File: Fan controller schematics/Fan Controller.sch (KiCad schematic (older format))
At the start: 9 parts, among them IC1 ATMEGA328-P, SW1 ROTARY_ENCODER, Y1 16MHz

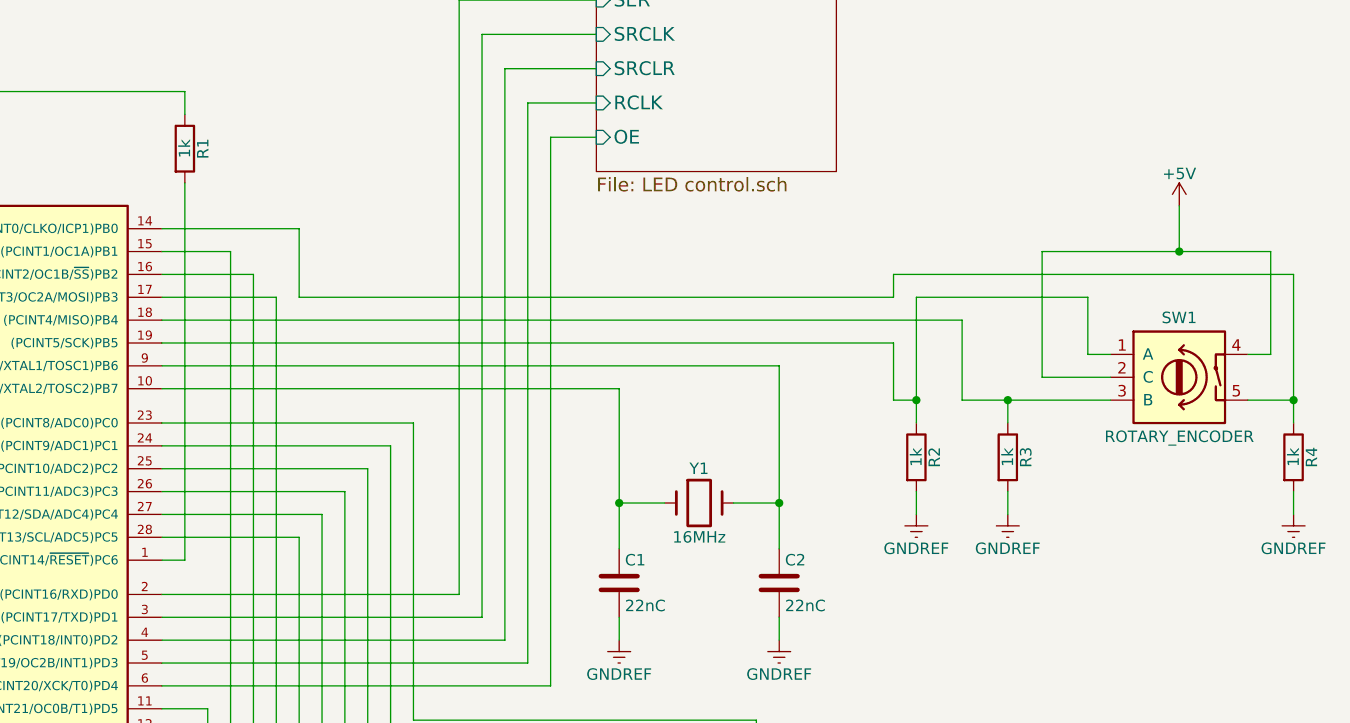
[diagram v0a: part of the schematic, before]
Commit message: Change rotary encoder to GND ref
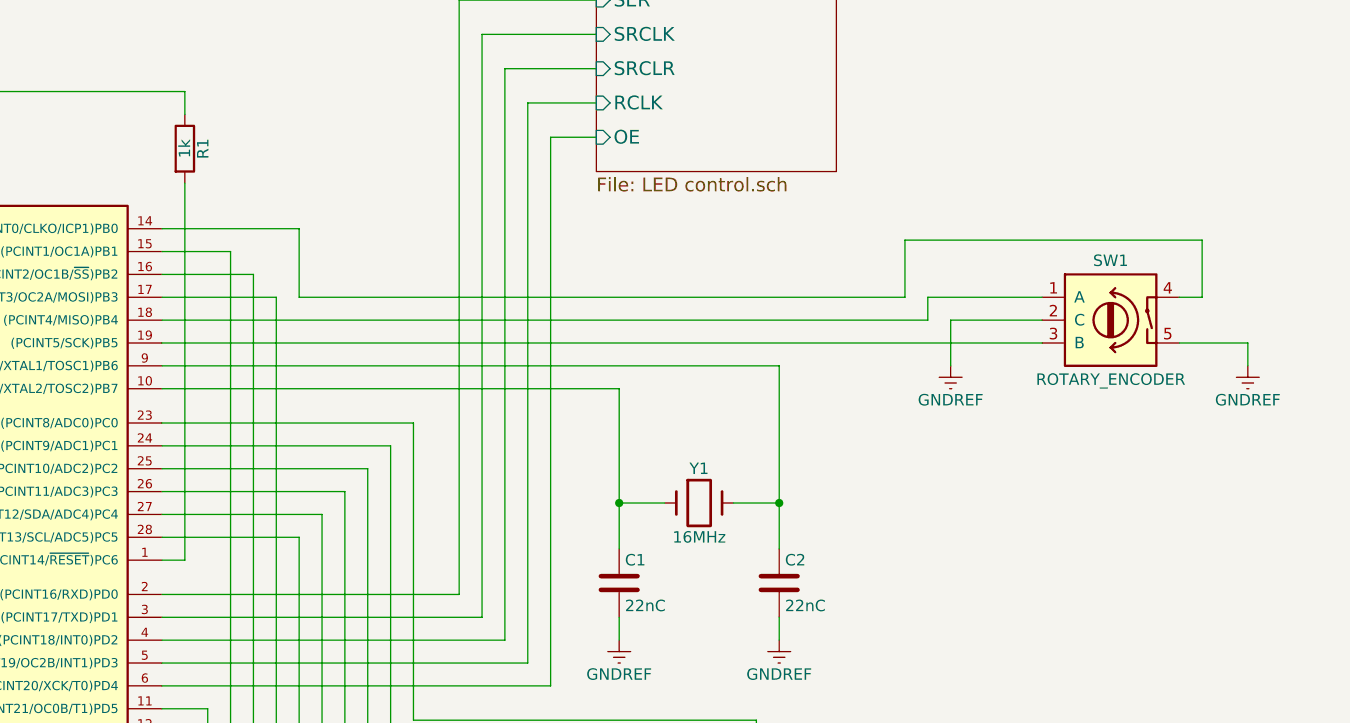
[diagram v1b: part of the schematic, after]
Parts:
- removed R2, R3, R4: 1k, symbol R
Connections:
- net +5V: no longer SW1.2 (C), SW1.4
- net GNDREF: now also SW1.2 (C), SW1.5
- net at IC1.14 ((PCINT0/CLKO/ICP1)PB0): now also SW1.4; no longer SW1.5
- net at IC1.18 ((PCINT4/MISO)PB4): now also SW1.1 (A); no longer SW1.3 (B)
- net at IC1.19 ((PCINT5/SCK)PB5): now also SW1.3 (B); no longer SW1.1 (A)
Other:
- moved on the sheet: SW1
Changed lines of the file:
@@
 Title "Fan Controller for PC"
 Date "2016-09-14"
-Rev "1.1"
+Rev "1.2"
 Comp "Dahlström Electronics"
 Comment1 ""
@@
 L ROTARY_ENCODER_SWITCH SW1
 U 1 1 57C35CD2
-P 8350 3450
-F 0 "SW1" H 8350 3710 50  0000 C CNN
-F 1 "ROTARY_ENCODER" H 8350 3190 50  0000 C CNN
-F 2 "" H 8250 3610 50  0001 C CNN
-F 3 "" H 8350 3710 50  0001 C CNN
-	1    8350 3450
+P 8050 3200
+F 0 "SW1" H 8050 3460 50  0000 C CNN
+F 1 "ROTARY_ENCODER" H 8050 2940 50  0000 C CNN
+F 2 "" H 7950 3360 50  0001 C CNN
+F 3 "" H 8050 3460 50  0001 C CNN
+	1    8050 3200
 	1    0    0    -1
 $EndComp
@@
 $EndComp
 $Comp
-L +5V #PWR7
-U 1 1 57DB623F
-P 8350 2700
-F 0 "#PWR7" H 8350 2550 50  0001 C CNN
-F 1 "+5V" H 8350 2840 50  0000 C CNN
-F 2 "" H 8350 2700 50  0000 C CNN
-F 3 "" H 8350 2700 50  0000 C CNN
-	1    8350 2700
-	1    0    0    -1
-$EndComp
-$Comp
-L R R2
-U 1 1 57DB6FA4
-P 7200 3800
-F 0 "R2" V 7280 3800 50  0000 C CNN
-F 1 "1k" V 7200 3800 50  0000 C CNN
-F 2 "" V 7130 3800 50  0000 C CNN
-F 3 "" H 7200 3800 50  0000 C CNN
-	1    7200 3800
-	1    0    0    -1
-$EndComp
-$Comp
-L R R3
-U 1 1 57DB70D7
-P 7600 3800
-F 0 "R3" V 7680 3800 50  0000 C CNN
-F 1 "1k" V 7600 3800 50  0000 C CNN
-F 2 "" V 7530 3800 50  0000 C CNN
-F 3 "" H 7600 3800 50  0000 C CNN
-	1    7600 3800
-	1    0    0    -1
-$EndComp
-$Comp
-L GNDREF #PWR5
-U 1 1 57DB7F2E
-P 7200 4050
-F 0 "#PWR5" H 7200 3800 50  0001 C CNN
-F 1 "GNDREF" H 7200 3900 50  0000 C CNN
-F 2 "" H 7200 4050 60  0000 C CNN
-F 3 "" H 7200 4050 60  0000 C CNN
-	1    7200 4050
-	1    0    0    -1
-$EndComp
-$Comp
-L GNDREF #PWR6
-U 1 1 57DB7FA8
-P 7600 4050
-F 0 "#PWR6" H 7600 3800 50  0001 C CNN
-F 1 "GNDREF" H 7600 3900 50  0000 C CNN
-F 2 "" H 7600 4050 60  0000 C CNN
-F 3 "" H 7600 4050 60  0000 C CNN
-	1    7600 4050
-	1    0    0    -1
-$EndComp
-$Comp
-L R R4
-U 1 1 57DB9C0A
-P 8850 3800
-F 0 "R4" V 8930 3800 50  0000 C CNN
-F 1 "1k" V 8850 3800 50  0000 C CNN
-F 2 "" V 8780 3800 50  0000 C CNN
-F 3 "" H 8850 3800 50  0000 C CNN
-	1    8850 3800
-	1    0    0    -1
-$EndComp
-$Comp
-L GNDREF #PWR8
-U 1 1 57DB9D63
-P 8850 4050
-F 0 "#PWR8" H 8850 3800 50  0001 C CNN
-F 1 "GNDREF" H 8850 3900 50  0000 C CNN
-F 2 "" H 8850 4050 60  0000 C CNN
-F 3 "" H 8850 4050 60  0000 C CNN
-	1    8850 4050
-	1    0    0    -1
-$EndComp
-$Comp
 L R R1
 U 1 1 57DBCB8F
@@
 	5600 2400 5800 2400
 Wire Wire Line
-	7750 2900 7750 3450
-Wire Wire Line
-	7750 3450 8050 3450
-Wire Wire Line
-	8050 3350 7950 3350
-Wire Wire Line
-	7950 3350 7950 3100
-Wire Wire Line
-	7950 3100 7200 3100
-Wire Wire Line
-	7200 3100 7200 3550
-Wire Wire Line
-	7200 3550 7200 3650
-Wire Wire Line
-	7400 3550 7600 3550
-Wire Wire Line
-	7600 3550 8050 3550
-Wire Wire Line
-	7600 3550 7600 3650
-Wire Wire Line
-	7400 3550 7400 3200
-Wire Wire Line
-	7400 3200 3900 3200
-Connection ~ 7600 3550
-Wire Wire Line
-	7200 3550 7100 3550
-Wire Wire Line
-	7100 3550 7100 3300
-Connection ~ 7200 3550
-Wire Wire Line
-	7100 3300 3900 3300
-Wire Wire Line
-	7600 3950 7600 4050
-Wire Wire Line
-	7200 3950 7200 4050
-Wire Wire Line
-	7750 2900 8350 2900
-Wire Wire Line
-	8350 2900 8750 2900
-Wire Wire Line
-	8350 2900 8350 2700
-Wire Wire Line
-	8650 3350 8750 3350
-Wire Wire Line
-	8750 3350 8750 2900
-Connection ~ 8350 2900
-Wire Wire Line
-	8650 3550 8850 3550
-Wire Wire Line
-	8850 3000 8850 3550
-Wire Wire Line
-	8850 3550 8850 3650
-Wire Wire Line
-	8850 3950 8850 4050
-Wire Wire Line
-	8850 3000 7100 3000
-Wire Wire Line
-	7100 3000 7100 3100
-Connection ~ 8850 3550
-Wire Wire Line
-	7100 3100 4500 3100
-Wire Wire Line
 	4500 3100 4500 2800
 Wire Wire Line
@@
 	4500 5550 1850 5550
 Connection ~ 1850 5550
+Wire Wire Line
+	4500 3100 7150 3100
+Wire Wire Line
+	3900 3300 7750 3300
+Wire Wire Line
+	3900 3200 7250 3200
+$Comp
+L GNDREF #PWR?
+U 1 1 57D90A53
+P 7350 3400
+F 0 "#PWR?" H 7350 3150 50  0001 C CNN
+F 1 "GNDREF" H 7350 3250 50  0000 C CNN
+F 2 "" H 7350 3400 60  0000 C CNN
+F 3 "" H 7350 3400 60  0000 C CNN
+	1    7350 3400
+	1    0    0    -1
+$EndComp
+Wire Wire Line
+	7750 3200 7350 3200
+Wire Wire Line
+	7350 3200 7350 3400
+Wire Wire Line
+	7250 3200 7250 3100
+Wire Wire Line
+	7250 3100 7750 3100
+$Comp
+L GNDREF #PWR?
+U 1 1 57D90E03
+P 8650 3400
+F 0 "#PWR?" H 8650 3150 50  0001 C CNN
+F 1 "GNDREF" H 8650 3250 50  0000 C CNN
+F 2 "" H 8650 3400 60  0000 C CNN
+F 3 "" H 8650 3400 60  0000 C CNN
+	1    8650 3400
+	1    0    0    -1
+$EndComp
+Wire Wire Line
+	8350 3300 8650 3300
+Wire Wire Line
+	8650 3300 8650 3400
+Wire Wire Line
+	7150 3100 7150 2850
+Wire Wire Line
+	7150 2850 8450 2850
+Wire Wire Line
+	8450 2850 8450 3100
+Wire Wire Line
+	8450 3100 8350 3100
 $EndSCHEMATC

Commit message: Small routing change
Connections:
- net GNDREF: now also IC1.13 ((PCINT23/AIN1)PD7)
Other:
- moved on the sheet: C1, C2, R1, SW1, Y1

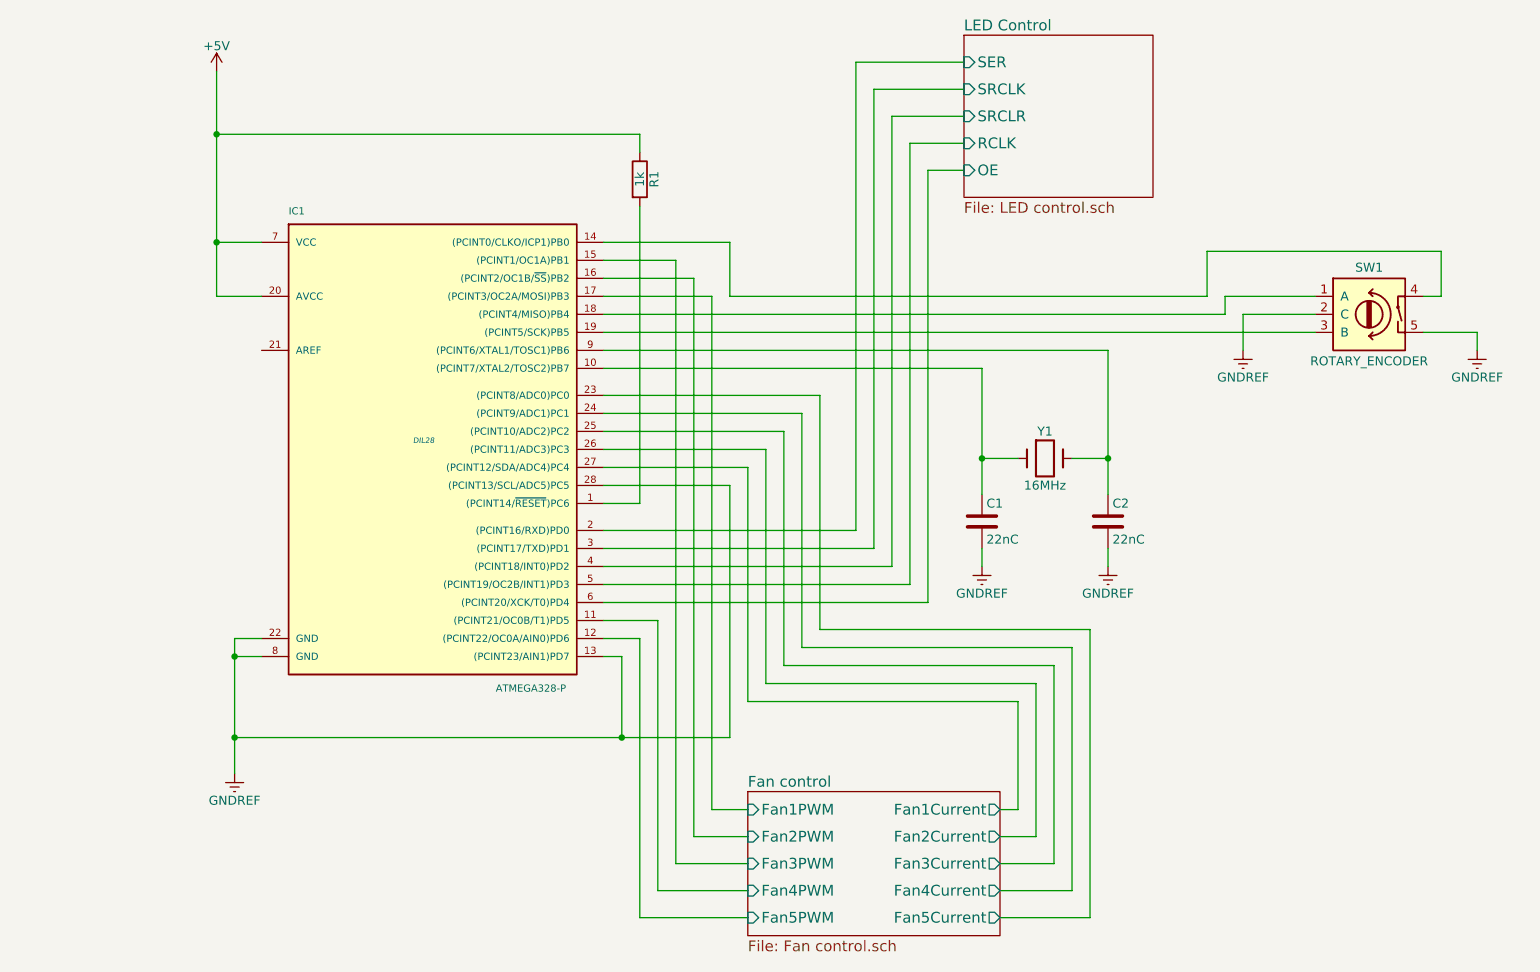
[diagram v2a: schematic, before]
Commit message: Add ADC filter and ref
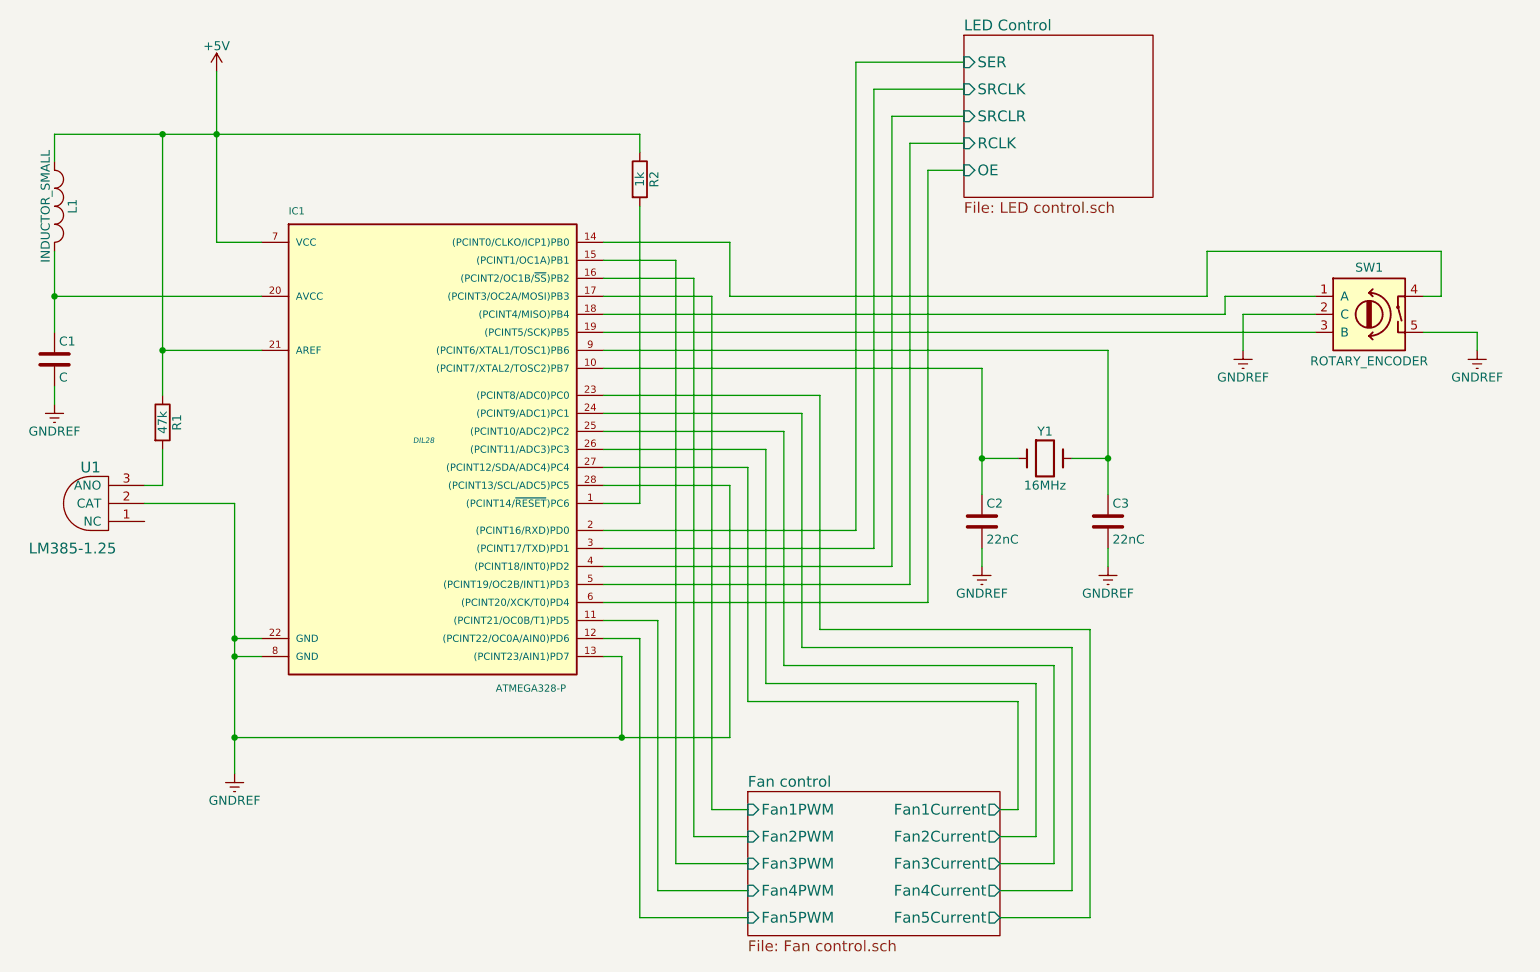
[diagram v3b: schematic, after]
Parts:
- added C1: C, symbol C
- added L1: INDUCTOR_SMALL, symbol INDUCTOR_SMALL
- added R1: 47k, symbol R
- added U1: LM385-1.25, symbol LM385-1.25
- renumbered C1 to C2, C2 to C3, R1 to R2
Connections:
- net +5V: now also IC1.21 (AREF), L1.1, R1.1; no longer IC1.20 (AVCC)
- net GNDREF: now also C1.2, U1.2 (CAT)
- new net: C1.1, IC1.20 (AVCC), L1.2
- new net: R1.2, U1.3 (ANO)
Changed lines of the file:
@@
 Title "Fan Controller for PC"
 Date "2016-09-14"
-Rev "1.2"
+Rev "1.3"
 Comp "Dahlström Electronics"
 Comment1 ""
@@
 $EndComp
 $Comp
-L +5V #PWR1
+L +5V #PWR2
 U 1 1 57C31247
 P 1750 1850
-F 0 "#PWR1" H 1750 1700 50  0001 C CNN
+F 0 "#PWR2" H 1750 1700 50  0001 C CNN
 F 1 "+5V" H 1750 1990 50  0000 C CNN
 F 2 "" H 1750 1850 60  0000 C CNN
@@
 $EndComp
 $Comp
-L GNDREF #PWR2
+L GNDREF #PWR3
 U 1 1 57C31302
 P 1850 5750
-F 0 "#PWR2" H 1850 5500 50  0001 C CNN
+F 0 "#PWR3" H 1850 5500 50  0001 C CNN
 F 1 "GNDREF" H 1850 5600 50  0000 C CNN
 F 2 "" H 1850 5750 60  0000 C CNN
@@
 $EndComp
 $Comp
-L C C1
+L C C2
 U 1 1 57DB00C1
 P 6000 4350
-F 0 "C1" H 6025 4450 50  0000 L CNN
+F 0 "C2" H 6025 4450 50  0000 L CNN
 F 1 "22nC" H 6025 4250 50  0000 L CNN
 F 2 "" H 6038 4200 50  0000 C CNN
@@
 $EndComp
 $Comp
-L C C2
+L C C3
 U 1 1 57DB0741
 P 6700 4350
-F 0 "C2" H 6725 4450 50  0000 L CNN
+F 0 "C3" H 6725 4450 50  0000 L CNN
 F 1 "22nC" H 6725 4250 50  0000 L CNN
 F 2 "" H 6738 4200 50  0000 C CNN
@@
 $EndComp
 $Comp
-L GNDREF #PWR3
+L GNDREF #PWR4
 U 1 1 57DB07CE
 P 6000 4600
-F 0 "#PWR3" H 6000 4350 50  0001 C CNN
+F 0 "#PWR4" H 6000 4350 50  0001 C CNN
 F 1 "GNDREF" H 6000 4450 50  0000 C CNN
 F 2 "" H 6000 4600 60  0000 C CNN
@@
 $EndComp
 $Comp
-L GNDREF #PWR4
+L GNDREF #PWR5
 U 1 1 57DB0842
 P 6700 4600
-F 0 "#PWR4" H 6700 4350 50  0001 C CNN
+F 0 "#PWR5" H 6700 4350 50  0001 C CNN
 F 1 "GNDREF" H 6700 4450 50  0000 C CNN
 F 2 "" H 6700 4600 60  0000 C CNN
@@
 $EndComp
 $Comp
-L R R1
+L R R2
 U 1 1 57DBCB8F
 P 4100 2450
-F 0 "R1" V 4180 2450 50  0000 C CNN
+F 0 "R2" V 4180 2450 50  0000 C CNN
 F 1 "1k" V 4100 2450 50  0000 C CNN
 F 2 "" V 4030 2450 50  0000 C CNN
@@
 $EndComp
 Wire Wire Line
-	1750 1850 1750 3100
-Wire Wire Line
 	1750 2800 2000 2800
 Wire Wire Line
 	2000 5000 1850 5000
 Wire Wire Line
-	1850 5000 1850 5750
+	1850 4250 1850 5750
 Wire Wire Line
 	2000 5100 1850 5100
 Connection ~ 1850 5100
 Wire Wire Line
-	1750 3100 2000 3100
-Connection ~ 1750 2800
+	850  3100 2000 3100
 Wire Wire Line
 	6000 3500 6000 4200
@@
 	4600 2800 3900 2800
 Wire Wire Line
-	4100 2300 4100 2200
-Wire Wire Line
-	4100 2200 1750 2200
+	4100 2200 4100 2300
+Wire Wire Line
+	850  2200 4100 2200
 Connection ~ 1750 2200
 Wire Wire Line
@@
 	3900 4150 4600 4150
 Wire Wire Line
-	4600 4150 4600 5550
-Wire Wire Line
-	4600 5550 1850 5550
+	4600 5550 4600 4150
+Wire Wire Line
+	1850 5550 4600 5550
 Connection ~ 1850 5550
 Wire Wire Line
@@
 	3900 3200 7350 3200
 $Comp
-L GNDREF #PWR?
+L GNDREF #PWR6
 U 1 1 57D90A53
 P 7450 3400
-F 0 "#PWR?" H 7450 3150 50  0001 C CNN
+F 0 "#PWR6" H 7450 3150 50  0001 C CNN
 F 1 "GNDREF" H 7450 3250 50  0000 C CNN
 F 2 "" H 7450 3400 60  0000 C CNN
@@
 	7350 3100 7850 3100
 $Comp
-L GNDREF #PWR?
+L GNDREF #PWR7
 U 1 1 57D90E03
 P 8750 3400
-F 0 "#PWR?" H 8750 3150 50  0001 C CNN
+F 0 "#PWR7" H 8750 3150 50  0001 C CNN
 F 1 "GNDREF" H 8750 3250 50  0000 C CNN
 F 2 "" H 8750 3400 60  0000 C CNN
@@
 	4000 5100 4000 5550
 Connection ~ 4000 5550
+$Comp
+L INDUCTOR_SMALL L1
+U 1 1 57D9448B
+P 850 2600
+F 0 "L1" H 850 2700 50  0000 C CNN
+F 1 "INDUCTOR_SMALL" H 850 2550 50  0000 C CNN
+F 2 "" H 850 2600 50  0000 C CNN
+F 3 "" H 850 2600 50  0000 C CNN
+	1    850  2600
+	0    1    1    0
+$EndComp
+$Comp
+L C C1
+U 1 1 57D94589
+P 850 3450
+F 0 "C1" H 875 3550 50  0000 L CNN
+F 1 "C" H 875 3350 50  0000 L CNN
+F 2 "" H 888 3300 50  0000 C CNN
+F 3 "" H 850 3450 50  0000 C CNN
+	1    850  3450
+	1    0    0    -1
+$EndComp
+Wire Wire Line
+	850  2850 850  3300
+Connection ~ 850  3100
+Wire Wire Line
+	850  2350 850  2200
+Wire Wire Line
+	1750 1850 1750 2800
+$Comp
+L GNDREF #PWR1
+U 1 1 57D95279
+P 850 3700
+F 0 "#PWR1" H 850 3450 50  0001 C CNN
+F 1 "GNDREF" H 850 3550 50  0000 C CNN
+F 2 "" H 850 3700 60  0000 C CNN
+F 3 "" H 850 3700 60  0000 C CNN
+	1    850  3700
+	1    0    0    -1
+$EndComp
+Wire Wire Line
+	850  3600 850  3700
+$Comp
+L LM385-1.25 U1
+U 1 1 57D96471
+P 800 4250
+F 0 "U1" V 1000 4000 60  0000 C CNN
+F 1 "LM385-1.25" V 550 4100 60  0000 C CNN
+F 2 "" H 800 4250 60  0001 C CNN
+F 3 "" H 800 4250 60  0001 C CNN
+	1    800  4250
+	0    -1   -1   0
+$EndComp
+Wire Wire Line
+	1350 4250 1850 4250
+Connection ~ 1850 5000
+$Comp
+L R R1
+U 1 1 57D96D6B
+P 1450 3800
+F 0 "R1" V 1530 3800 50  0000 C CNN
+F 1 "47k" V 1450 3800 50  0000 C CNN
+F 2 "" V 1380 3800 50  0000 C CNN
+F 3 "" H 1450 3800 50  0000 C CNN
+	1    1450 3800
+	1    0    0    -1
+$EndComp
+Wire Wire Line
+	1450 2200 1450 3650
+Connection ~ 1450 2200
+Wire Wire Line
+	1450 3950 1450 4150
+Wire Wire Line
+	1450 4150 1350 4150
+Wire Wire Line
+	2000 3400 1450 3400
+Connection ~ 1450 3400
 $EndSCHEMATC

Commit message: Update component values
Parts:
- C1: value C -> 100nF
- L1: value INDUCTOR_SMALL -> 10µH
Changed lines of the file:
@@
 P 850 2600
 F 0 "L1" H 850 2700 50  0000 C CNN
-F 1 "INDUCTOR_SMALL" H 850 2550 50  0000 C CNN
+F 1 "10µH" H 850 2550 50  0000 C CNN
 F 2 "" H 850 2600 50  0000 C CNN
 F 3 "" H 850 2600 50  0000 C CNN
@@
 P 850 3450
 F 0 "C1" H 875 3550 50  0000 L CNN
-F 1 "C" H 875 3350 50  0000 L CNN
+F 1 "100nF" H 875 3350 50  0000 L CNN
 F 2 "" H 888 3300 50  0000 C CNN
 F 3 "" H 850 3450 50  0000 C CNN
